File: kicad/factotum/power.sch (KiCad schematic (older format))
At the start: 20 parts

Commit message: working on schematic
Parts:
- removed FB? (x2): Ferrite_Bead, symbol Device:Ferrite_Bead_Small
- gave numbers to parts that had none: 18
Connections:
- net +12V: now also C13.1, C15.1, D1.1 (K), L1.1, U3.3 (VI)
- net -12V: now also D2.2 (A)

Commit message: initial layout of top board
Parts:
- C10, C11, C12, C13, C14, C15, C16, C17, C18, C19: footprint (none) -> Capacitor_SMD:C_0603_1608Metric_Pad1.08x0.95mm_HandSolder
- D3: footprint (none) -> Package_TO_SOT_SMD:SOT-23
- J3: footprint (none) -> Connector_PinSocket_1.27mm:PinSocket_2x05_P1.27mm_Vertical
- L1: footprint (none) -> Inductor_SMD:L_0201_0603Metric_Pad0.64x0.40mm_HandSolder
- R12: footprint (none) -> Resistor_SMD:R_0201_0603Metric_Pad0.64x0.40mm_HandSolder
- U3: footprint (none) -> Package_TO_SOT_SMD:SOT-89-3
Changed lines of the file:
@@
 F 0 "U3" H 5300 2915 50  0000 C CNN
 F 1 "LD2981ABU33" H 5300 2824 50  0000 C CNN
-F 2 "" H 5300 2650 50  0001 C CNN
+F 2 "Package_TO_SOT_SMD:SOT-89-3" H 5300 2650 50  0001 C CNN
 F 3 "" H 5300 2650 50  0001 C CNN
 	1    5300 2650
@@
 F 0 "C19" H 6241 2796 50  0000 L CNN
 F 1 "10u" H 6241 2705 50  0000 L CNN
-F 2 "" H 6150 2750 50  0001 C CNN
+F 2 "Capacitor_SMD:C_0603_1608Metric_Pad1.08x0.95mm_HandSolder" H 6150 2750 50  0001 C CNN
 F 3 "~" H 6150 2750 50  0001 C CNN
 	1    6150 2750
@@
 F 0 "C18" H 6241 1746 50  0000 L CNN
 F 1 "10u" H 6241 1655 50  0000 L CNN
-F 2 "" H 6150 1700 50  0001 C CNN
+F 2 "Capacitor_SMD:C_0603_1608Metric_Pad1.08x0.95mm_HandSolder" H 6150 1700 50  0001 C CNN
 F 3 "~" H 6150 1700 50  0001 C CNN
 	1    6150 1700
@@
 F 0 "C16" H 5892 1746 50  0000 L CNN
 F 1 "100n" H 5892 1655 50  0000 L CNN
-F 2 "" H 5800 1700 50  0001 C CNN
+F 2 "Capacitor_SMD:C_0603_1608Metric_Pad1.08x0.95mm_HandSolder" H 5800 1700 50  0001 C CNN
 F 3 "~" H 5800 1700 50  0001 C CNN
 	1    5800 1700
@@
 F 0 "C17" H 5891 2796 50  0000 L CNN
 F 1 "10u" H 5891 2705 50  0000 L CNN
-F 2 "" H 5800 2750 50  0001 C CNN
+F 2 "Capacitor_SMD:C_0603_1608Metric_Pad1.08x0.95mm_HandSolder" H 5800 2750 50  0001 C CNN
 F 3 "~" H 5800 2750 50  0001 C CNN
 	1    5800 2750
@@
 F 0 "C14" H 4892 1746 50  0000 L CNN
 F 1 "22u" H 4892 1655 50  0000 L CNN
-F 2 "" H 4800 1700 50  0001 C CNN
+F 2 "Capacitor_SMD:C_0603_1608Metric_Pad1.08x0.95mm_HandSolder" H 4800 1700 50  0001 C CNN
 F 3 "~" H 4800 1700 50  0001 C CNN
 	1    4800 1700
@@
 F 0 "C13" H 4492 1746 50  0000 L CNN
 F 1 "22u" H 4492 1655 50  0000 L CNN
-F 2 "" H 4400 1700 50  0001 C CNN
+F 2 "Capacitor_SMD:C_0603_1608Metric_Pad1.08x0.95mm_HandSolder" H 4400 1700 50  0001 C CNN
 F 3 "~" H 4400 1700 50  0001 C CNN
 	1    4400 1700
@@
 F 0 "C15" H 4942 2796 50  0000 L CNN
 F 1 "22u" H 4942 2705 50  0000 L CNN
-F 2 "" H 4850 2750 50  0001 C CNN
+F 2 "Capacitor_SMD:C_0603_1608Metric_Pad1.08x0.95mm_HandSolder" H 4850 2750 50  0001 C CNN
 F 3 "~" H 4850 2750 50  0001 C CNN
 	1    4850 2750
@@
 F 0 "L1" V 4785 1600 50  0000 C CNN
 F 1 "33u" V 4694 1600 50  0000 C CNN
-F 2 "" H 4600 1600 50  0001 C CNN
+F 2 "Inductor_SMD:L_0201_0603Metric_Pad0.64x0.40mm_HandSolder" H 4600 1600 50  0001 C CNN
 F 3 "~" H 4600 1600 50  0001 C CNN
 	1    4600 1600
@@
 F 0 "J3" H 1700 1875 50  0000 C CNN
 F 1 "Conn_02x05_Odd_Even" H 1700 1966 50  0000 C CNN
-F 2 "" H 1650 2300 50  0001 C CNN
+F 2 "Connector_PinSocket_1.27mm:PinSocket_2x05_P1.27mm_Vertical" H 1650 2300 50  0001 C CNN
 F 3 "~" H 1650 2300 50  0001 C CNN
 	1    1650 2300
@@
 F 0 "C10" H 3141 2146 50  0000 L CNN
 F 1 "22u" H 3141 2055 50  0000 L CNN
-F 2 "" H 3050 2100 50  0001 C CNN
+F 2 "Capacitor_SMD:C_0603_1608Metric_Pad1.08x0.95mm_HandSolder" H 3050 2100 50  0001 C CNN
 F 3 "~" H 3050 2100 50  0001 C CNN
 	1    3050 2100
@@
 F 0 "C11" H 3141 2546 50  0000 L CNN
 F 1 "22u" H 3141 2455 50  0000 L CNN
-F 2 "" H 3050 2500 50  0001 C CNN
+F 2 "Capacitor_SMD:C_0603_1608Metric_Pad1.08x0.95mm_HandSolder" H 3050 2500 50  0001 C CNN
 F 3 "~" H 3050 2500 50  0001 C CNN
 	1    3050 2500
@@
 F 0 "R12" V 3404 3350 50  0000 C CNN
 F 1 "1.5k" V 3495 3350 50  0000 C CNN
-F 2 "" H 3600 3350 50  0001 C CNN
+F 2 "Resistor_SMD:R_0201_0603Metric_Pad0.64x0.40mm_HandSolder" H 3600 3350 50  0001 C CNN
 F 3 "~" H 3600 3350 50  0001 C CNN
 	1    3600 3350
@@
 F 0 "D3" V 3946 3380 50  0000 R CNN
 F 1 "LM4040B10" V 3850 3950 50  0000 R CNN
-F 2 "" V 3900 3450 50  0001 C CNN
+F 2 "Package_TO_SOT_SMD:SOT-23" V 3900 3450 50  0001 C CNN
 F 3 "~" V 3900 3450 50  0001 C CNN
 	1    3900 3450
@@
 F 0 "C12" H 4242 3496 50  0000 L CNN
 F 1 "1u" H 4242 3405 50  0000 L CNN
-F 2 "" H 4150 3450 50  0001 C CNN
+F 2 "Capacitor_SMD:C_0603_1608Metric_Pad1.08x0.95mm_HandSolder" H 4150 3450 50  0001 C CNN
 F 3 "~" H 4150 3450 50  0001 C CNN
 	1    4150 3450

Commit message: inital board layout done but not routed
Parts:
- J3: footprint Connector_PinSocket_1.27mm:PinSocket_2x05_P1.27mm_Vertical -> Connector_PinHeader_2.54mm:PinHeader_2x05_P2.54mm_Vertical
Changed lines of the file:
@@
 F 0 "J3" H 1700 1875 50  0000 C CNN
 F 1 "Conn_02x05_Odd_Even" H 1700 1966 50  0000 C CNN
-F 2 "Connector_PinSocket_1.27mm:PinSocket_2x05_P1.27mm_Vertical" H 1650 2300 50  0001 C CNN
+F 2 "Connector_PinHeader_2.54mm:PinHeader_2x05_P2.54mm_Vertical" H 1650 2300 50  0001 C CNN
 F 3 "~" H 1650 2300 50  0001 C CNN
 	1    1650 2300

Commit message: adding switches to inputs; fixing resistor components to 603
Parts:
- R12: footprint Resistor_SMD:R_0201_0603Metric_Pad0.64x0.40mm_HandSolder -> Resistor_SMD:R_0603_1608Metric_Pad0.98x0.95mm_HandSolder
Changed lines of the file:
@@
 F 0 "R12" V 3404 3350 50  0000 C CNN
 F 1 "1.5k" V 3495 3350 50  0000 C CNN
-F 2 "Resistor_SMD:R_0201_0603Metric_Pad0.64x0.40mm_HandSolder" H 3600 3350 50  0001 C CNN
+F 2 "Resistor_SMD:R_0603_1608Metric_Pad0.98x0.95mm_HandSolder" H 3600 3350 50  0001 C CNN
 F 3 "~" H 3600 3350 50  0001 C CNN
 	1    3600 3350

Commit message: layout components again
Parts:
- L1: footprint Inductor_SMD:L_0201_0603Metric_Pad0.64x0.40mm_HandSolder -> Inductor_SMD:L_0603_1608Metric_Pad1.05x0.95mm_HandSolder
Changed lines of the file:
@@
 F 0 "L1" V 4785 1600 50  0000 C CNN
 F 1 "33u" V 4694 1600 50  0000 C CNN
-F 2 "Inductor_SMD:L_0201_0603Metric_Pad0.64x0.40mm_HandSolder" H 4600 1600 50  0001 C CNN
+F 2 "Inductor_SMD:L_0603_1608Metric_Pad1.05x0.95mm_HandSolder" H 4600 1600 50  0001 C CNN
 F 3 "~" H 4600 1600 50  0001 C CNN
 	1    4600 1600

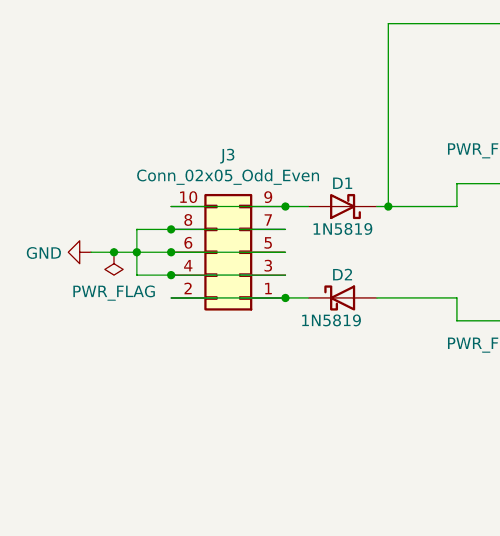
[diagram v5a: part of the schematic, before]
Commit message: working on pcd routing
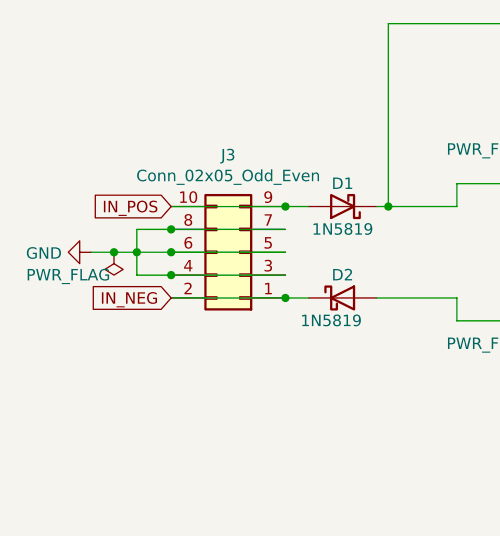
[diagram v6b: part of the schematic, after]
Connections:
- net IN_NEG: now reaches D2.1 (K), J3.1 (Pin_1), J3.2 (Pin_2)
- net IN_POS: now reaches D1.2 (A), J3.10 (Pin_10), J3.9 (Pin_9)
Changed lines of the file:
@@
 P 1100 2300
 F 0 "#FLG0103" H 1100 2375 50  0001 C CNN
-F 1 "PWR_FLAG" H 1100 2473 50  0000 C CNN
+F 1 "PWR_FLAG" H 1300 2400 50  0000 C CNN
 F 2 "" H 1100 2300 50  0001 C CNN
 F 3 "~" H 1100 2300 50  0001 C CNN
@@
 Wire Wire Line
 	4150 3250 4150 3350
+Text GLabel 1350 2100 0    50   Input ~ 0
+IN_POS
+Text GLabel 1350 2500 0    50   Input ~ 0
+IN_NEG
 $EndSCHEMATC

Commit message: more work on routing
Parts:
- renumbered D2 to D10, D3 to D11, D1 to D9
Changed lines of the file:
@@
 $EndComp
 $Comp
-L Diode:1N5819 D2
+L Diode:1N5819 D10
 U 1 1 60621C3D
 P 2100 2500
-F 0 "D2" H 2100 2600 50  0000 C CNN
+F 0 "D10" H 2100 2600 50  0000 C CNN
 F 1 "1N5819" H 2050 2400 50  0000 C CNN
 F 2 "Diode_THT:D_DO-41_SOD81_P10.16mm_Horizontal" H 2100 2325 50  0001 C CNN
@@
 $EndComp
 $Comp
-L Diode:1N5819 D1
+L Diode:1N5819 D9
 U 1 1 60622508
 P 2100 2100
-F 0 "D1" H 2100 2000 50  0000 C CNN
+F 0 "D9" H 2100 2000 50  0000 C CNN
 F 1 "1N5819" H 2100 2200 50  0000 C CNN
 F 2 "Diode_THT:D_DO-41_SOD81_P10.16mm_Horizontal" H 2100 1925 50  0001 C CNN
@@
 $EndComp
 $Comp
-L Device:D_Schottky_Small D3
+L Device:D_Schottky_Small D11
 U 1 1 6066AF76
 P 3900 3450
-F 0 "D3" V 3946 3380 50  0000 R CNN
+F 0 "D11" V 3946 3380 50  0000 R CNN
 F 1 "LM4040B10" V 3850 3950 50  0000 R CNN
 F 2 "Package_TO_SOT_SMD:SOT-23" V 3900 3450 50  0001 C CNN
